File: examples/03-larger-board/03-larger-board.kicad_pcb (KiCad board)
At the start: 2 copper layers, 80.4 x 43.2 mm, 25 parts, among them J1 DB25MALE, J2 DB9MALE, P1 CONN_6, U1 74LS125, U2 74LS125

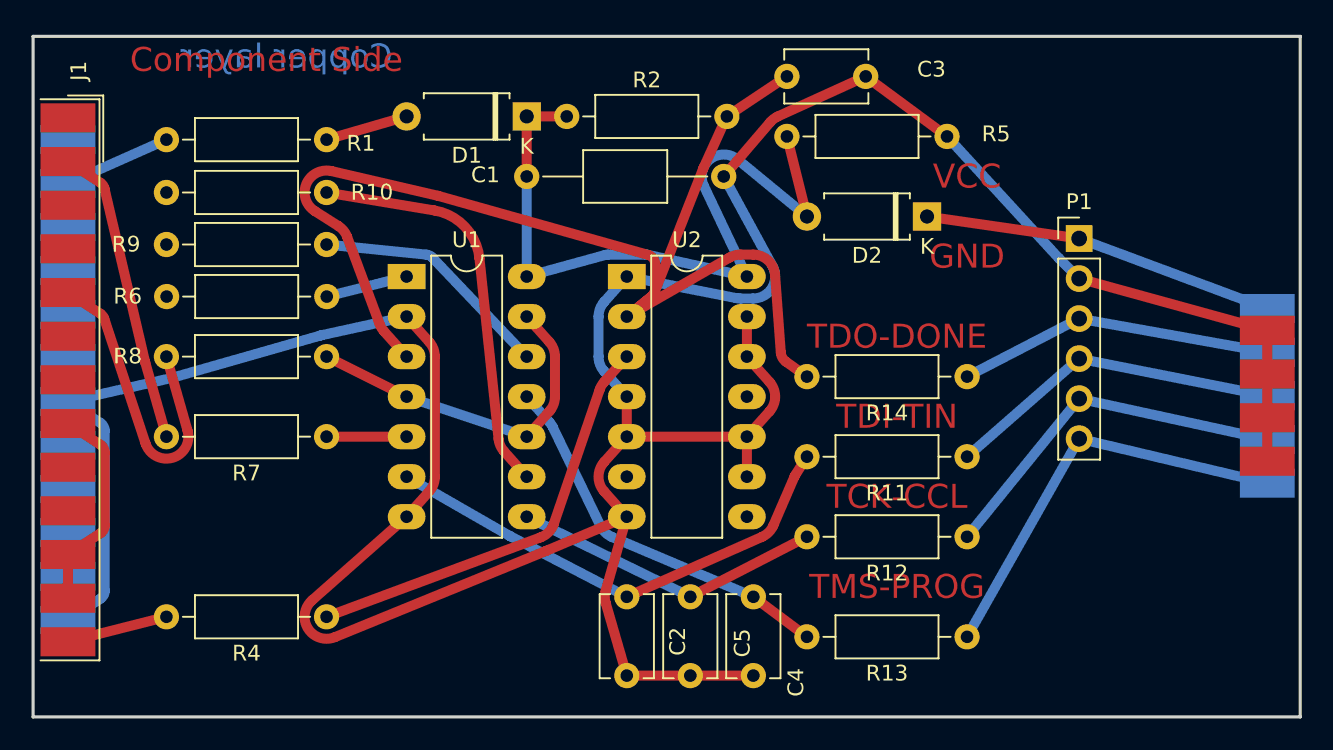
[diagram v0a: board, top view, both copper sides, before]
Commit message: feat(relax): settle every band at once instead of counting gaps
Replaces the portal/capacity/slot machinery with the direct thing it was
approximating. A board's copper is one arrangement, not a sequence of
decisions, so every band is re-solved against the *previous* positions of
all the others and all of them move together. Two bands contending for
the same space now both give way, which no ordering or rip-up can
produce.

The portals were scaffolding built to fake simultaneity, and they only
ever covered contention inside a narrow gap between two static obstacles.
Measurement showed why that was not enough: contention costs 30.4% of
ideal length on ecc83-pp and the slot model recovered none of it, because
the bands that detour are detouring around other *bands*, in open copper,
where no such gap exists.

Which layer a band sits on is settled in the same loop. Fixing it
beforehand -- each connection taking whichever layer was shortest for it
alone -- puts every band on one face, which the relaxation is then good
enough to make work while being materially longer than spreading out.

An earlier version also annealed the band-to-band clearance from soft to
solid, arguing that the taut solver treats other copper as walls and
walls do not yield. The argument is sound and the effect is nil: the
finished route on ecc83-pp is identical at 0.30, 0.60 and 1.00 hardness.
Bands have room to go around each other far more often than they need to
pass through, so the softening is gone rather than kept on a plausible
story.

Sequential settling versus joint relaxation, same boards, same process:

  ecc83-pp F.Cu        19/20  305.3mm  ->  20/20  292.9mm
  ecc83-pp F.Cu+B.Cu   20/20  239.5mm  ->  20/20  239.5mm
  sonde xilinx         63/66  690.3mm  ->  64/66  678.4mm

Where there is headroom it wins on both counts -- more connections
finished and less copper -- which is the tell that it is doing the right
thing rather than merely doing something. Zero DRC errors throughout.

Relax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
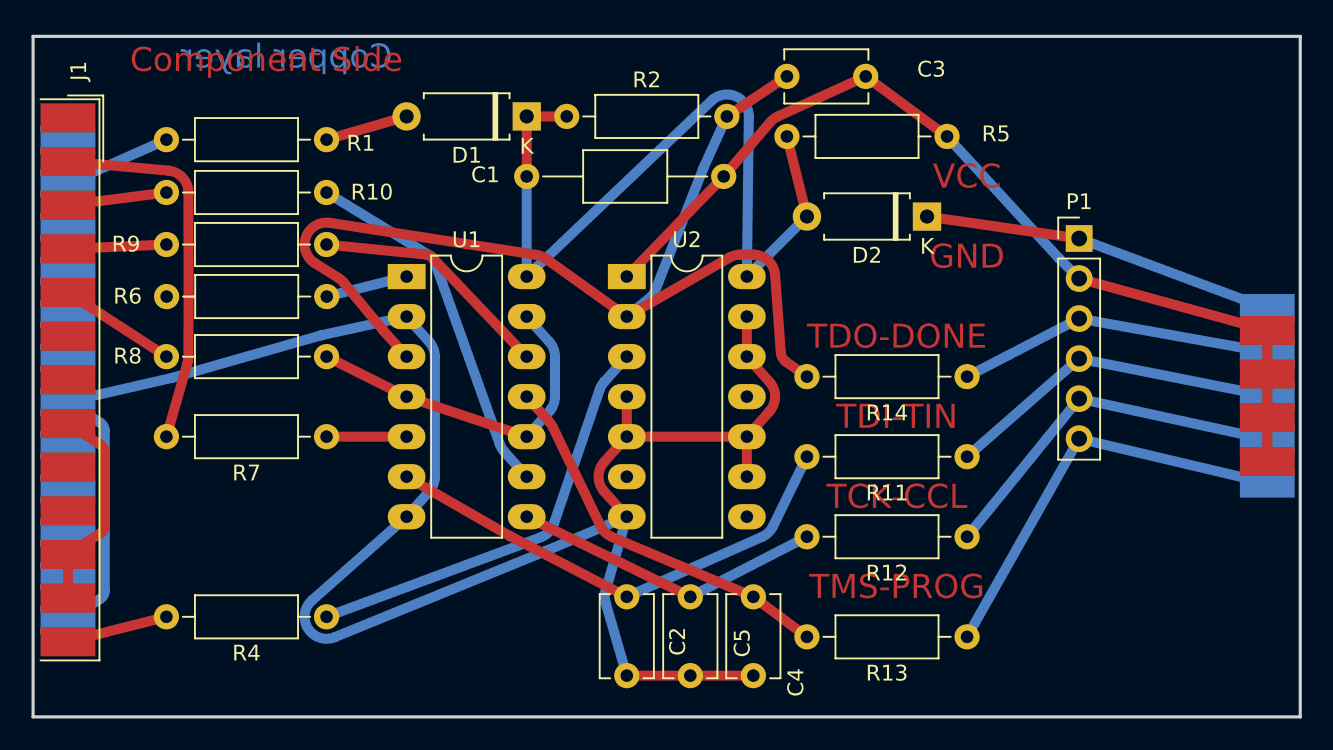
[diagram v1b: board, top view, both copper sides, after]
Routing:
- net GND: track 207.4 -> 189.9 mm
- net /CTRL-D3: track 20.0 -> 7.46 mm
- net Net-(U1A-O): track 77.9 -> 69.5 mm
- net /CLK-D1: track 0.00 -> 6.30 mm
- net /TMS-PROG-D2: track 0.00 -> 6.25 mm
- net VCC: track 47.8 -> 52.8 mm
- net /TDI-DIN-D0: track 19.1 -> 24.1 mm
- net Net-(U1C-D): track 25.9 -> 23.2 mm

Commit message: feat(route): a connection that cannot fit rips up what is blocking it
Every board is now fully routed and DRC clean:

  ecc83-pp F.Cu        20/20  292.9mm
  ecc83-pp F.Cu+B.Cu   20/20  239.5mm
  sonde xilinx         66/66  785.5mm    (was 64/66)

The two connections that were being dropped on sonde xilinx -- one of
them GND -- were not failing for want of a path. Routed alone, against
nothing but pads and the board edge, every one of their MST edges solves
on both layers. The tangent solver was refusing nothing.

The fault was that the settling pass placed connections longest-first
and never revisited one. Relaxation moves every band at once and gets
the arrangement close, but the endgame was strictly one-directional, so
whatever arrived last at a busy spot got whatever was left -- and if
that was nothing it was dropped, while a path plainly existed and
another net was merely sitting on it.

A connection that cannot be placed now identifies the settled copper
blocking it, takes the space, and hands the displaced connections back
to the queue to find somewhere else. Three rip-ups finish sonde xilinx.

The cost is length: 678mm to 785mm, because the two recovered
connections and the bands they displaced all take longer routes. A
complete board is worth more than a short one.

Rip-ups are budgeted at forty per board so a pair cannot trade the same
space forever. That is a stopping rule, not a convergence argument, and
nothing here bounds how far the result sits from the best arrangement.

35 tests pass, though the suite now takes 20 minutes -- routing the
dense board end to end is most of it.

Co-Authored-By: Claude Opus 5 <noreply@anthropic.com>
Claude-Session: https://claude.ai/code/session_01KugHz6rjbu6ieweNYBXF9n
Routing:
- net Net-(U1A-O): track 69.5 -> 143.9 mm
- net /TD0-PROG-D4: track 0.00 -> 12.9 mm
- net /TDI-DIN-D0: track 24.1 -> 35.0 mm
- net GND: track 189.9 -> 198.8 mm
